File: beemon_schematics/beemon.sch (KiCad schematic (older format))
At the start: 16 parts, among them SW1 SW_SPST, U1 TP4056mini, U2 AMS1117, U3 HD44780_I2C, U4 NodeMCU_1.0_(ESP-12E), U5 HX711

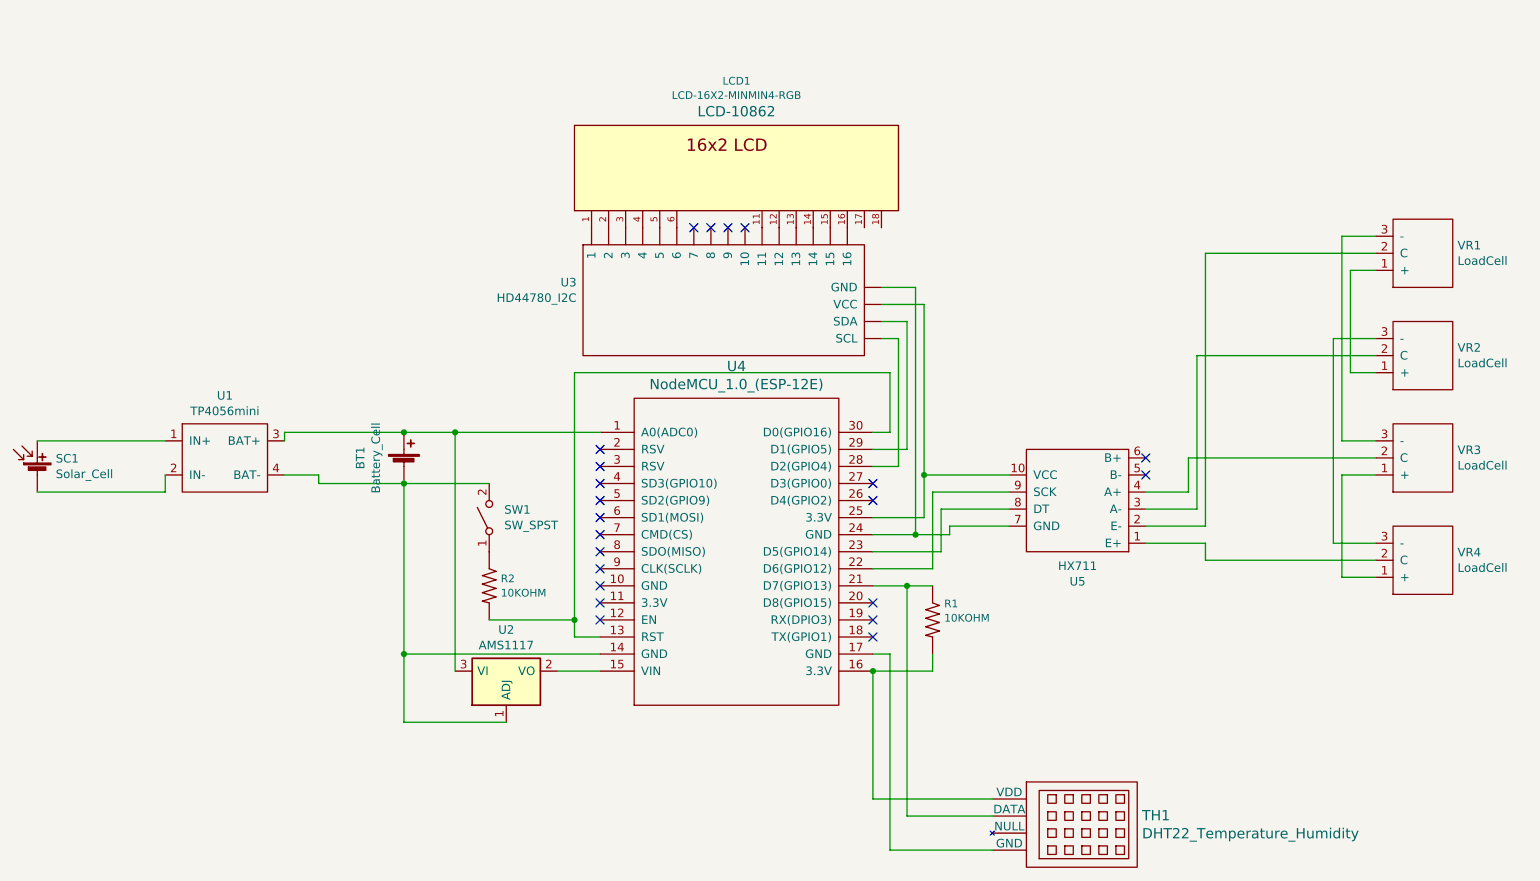
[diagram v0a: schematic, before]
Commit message: Code fixed and tested on 1st prototype. Schematics modified.
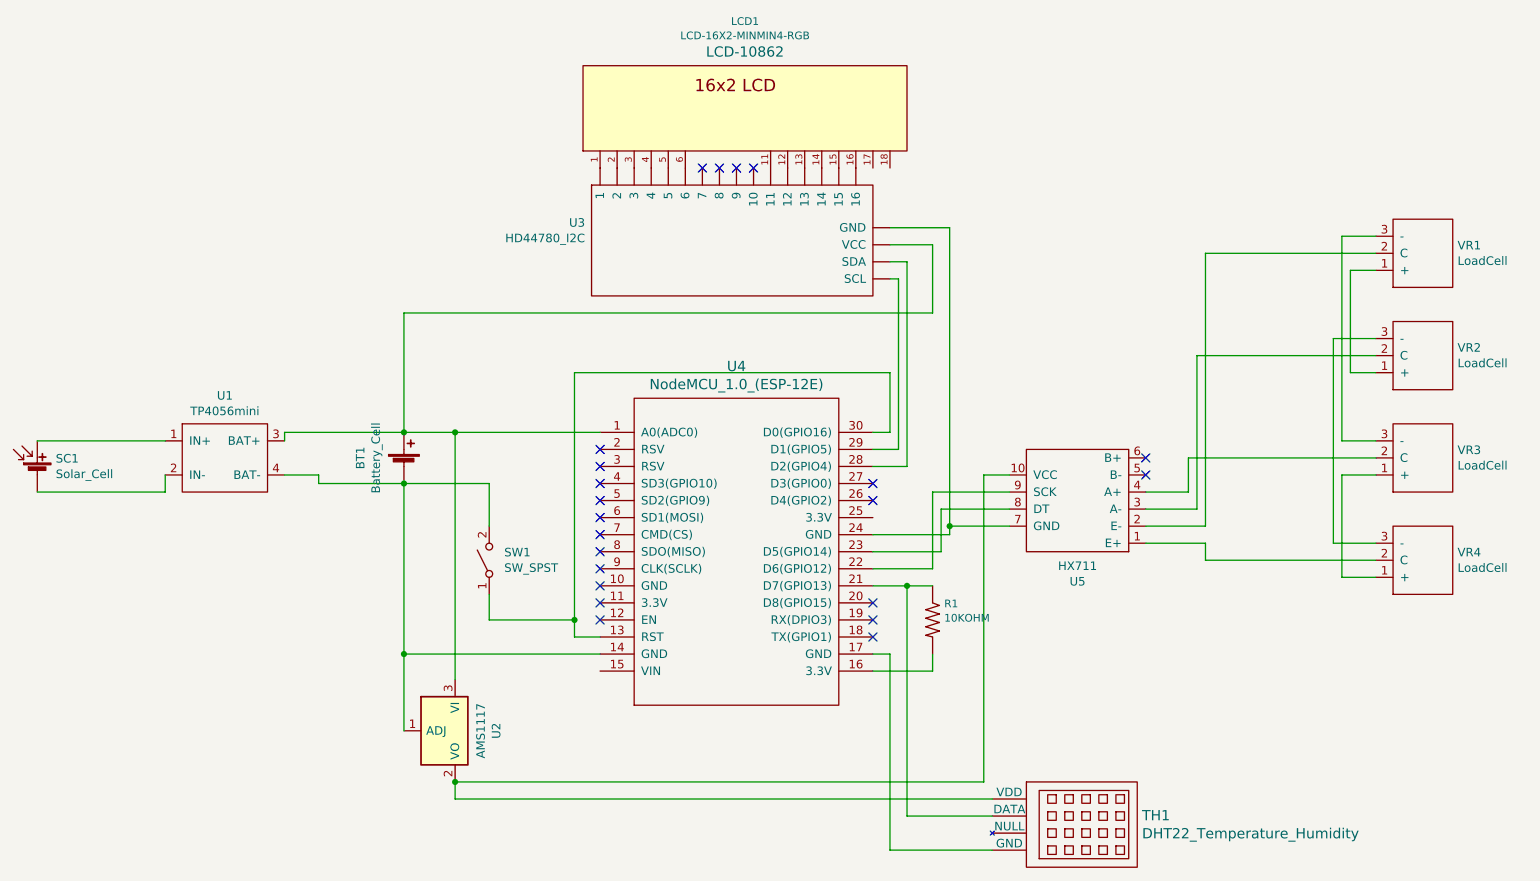
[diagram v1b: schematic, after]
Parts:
- removed R2: 10KOHM, AXIAL-0.3, symbol SparkFun-Resistors:10KOHM-HORIZ-1_4W-1%
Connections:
- net at BT1.1 (+), U1.3 (BAT+), U2.3 (VI)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: now also U3.~ (VCC)
- net at U4.13 (RST), U4.30 (D0(GPIO16)): now also SW1.1 (A)
- net at U4.15 (VIN): no longer U2.2 (VO)
- net at R1.P$2 (2), U4.16 (3.3V): no longer TH1.1 (VDD)
- new net: TH1.1 (VDD), U2.2 (VO), U5.10 (VCC)
- now unconnected: U3.~ (VCC), U4.25 (3.3V)
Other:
- moved on the sheet: LCD1, SW1, U2, U3
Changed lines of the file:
@@
 L Regulator_Linear:AMS1117 U2
 U 1 1 60756942
-P 4450 4950
-F 0 "U2" H 4450 5192 50  0000 C CNN
-F 1 "AMS1117" H 4450 5101 50  0000 C CNN
-F 2 "Package_TO_SOT_SMD:SOT-223-3_TabPin2" H 4450 5150 50  0001 C CNN
-F 3 "http://www.advanced-monolithic.com/pdf/ds1117.pdf" H 4550 4700 50  0001 C CNN
-	1    4450 4950
-	1    0    0    -1
+P 4150 5300
+F 0 "U2" H 4150 5542 50  0000 C CNN
+F 1 "AMS1117" H 4150 5451 50  0000 C CNN
+F 2 "Package_TO_SOT_SMD:SOT-223-3_TabPin2" H 4150 5500 50  0001 C CNN
+F 3 "http://www.advanced-monolithic.com/pdf/ds1117.pdf" H 4250 5050 50  0001 C CNN
+	1    4150 5300
+	0    1    1    0
 $EndComp
 $Comp
@@
 $EndComp
 Wire Wire Line
-	5000 3550 4150 3550
-Wire Wire Line
 	3850 3550 3150 3550
 Wire Wire Line
@@
 Connection ~ 3850 3850
 Wire Wire Line
-	3850 3550 4150 3550
-Connection ~ 4150 3550
-Wire Wire Line
-	4150 3550 4150 4950
-Wire Wire Line
-	4750 4950 5000 4950
-Wire Wire Line
-	4450 5250 3850 5250
-Wire Wire Line
-	3850 5250 3850 4850
-Connection ~ 3850 4850
-Wire Wire Line
 	1700 3600 2450 3600
 Wire Wire Line
 	1700 3900 2450 3900
-Wire Wire Line
-	6600 4950 6600 5700
-Wire Wire Line
-	6600 5700 7300 5700
 Wire Wire Line
 	6600 4850 6700 4850
@@
 Wire Wire Line
 	6950 4950 6600 4950
-Connection ~ 6600 4950
 Wire Wire Line
 	9550 2600 9400 2600
@@
 	7050 4100 7050 4150
 Wire Wire Line
-	7050 4150 6850 4150
-Wire Wire Line
 	7400 4000 7000 4000
 Wire Wire Line
@@
 	7000 4250 6600 4250
 Wire Wire Line
-	7400 3900 6950 3900
-Wire Wire Line
 	6950 3900 6950 4350
 Wire Wire Line
 	6950 4350 6600 4350
-Wire Wire Line
-	6600 4050 6900 4050
-Wire Wire Line
-	6900 3800 7400 3800
-Wire Wire Line
-	6900 2800 6900 3800
-Connection ~ 6900 3800
-Wire Wire Line
-	6900 3800 6900 4050
-Wire Wire Line
-	6850 2700 6850 4150
-Connection ~ 6850 4150
-Wire Wire Line
-	6850 4150 6600 4150
-Wire Wire Line
-	6800 2900 6800 3650
-Wire Wire Line
-	6800 3650 6600 3650
-Wire Wire Line
-	6750 3000 6750 3750
-Wire Wire Line
-	6750 3750 6600 3750
 NoConn ~ 5000 3650
 NoConn ~ 5000 3750
@@
 L Switch:SW_SPST SW1
 U 1 1 607C3174
-P 4350 4050
-F 0 "SW1" V 4396 3962 50  0000 R CNN
-F 1 "SW_SPST" V 4305 3962 50  0000 R CNN
-F 2 "" H 4350 4050 50  0001 C CNN
-F 3 "~" H 4350 4050 50  0001 C CNN
-	1    4350 4050
-	0    -1   -1   0
-$EndComp
-$Comp
-L SparkFun-Resistors:10KOHM-HORIZ-1_4W-1% R2
-U 1 1 607C4ED1
-P 4350 4450
-F 0 "R2" V 4308 4518 45  0000 L CNN
-F 1 "10KOHM" V 4392 4518 45  0000 L CNN
-F 2 "AXIAL-0.3" H 4350 4600 20  0001 C CNN
-F 3 "" H 4350 4450 60  0001 C CNN
-F 4 "" V 4434 4518 60  0000 L CNN "Field4"
-	1    4350 4450
-	0    1    1    0
+P 4350 4300
+F 0 "SW1" V 4396 4212 50  0000 R CNN
+F 1 "SW_SPST" V 4305 4212 50  0000 R CNN
+F 2 "" H 4350 4300 50  0001 C CNN
+F 3 "~" H 4350 4300 50  0001 C CNN
+	1    4350 4300
+	0    -1   -1   0
 $EndComp
 Wire Wire Line
@@
 Wire Wire Line
 	4350 3850 3850 3850
-Wire Wire Line
-	6650 2800 6900 2800
-Wire Wire Line
-	6650 2900 6800 2900
-Wire Wire Line
-	6650 3000 6750 3000
-Wire Wire Line
-	6650 2700 6850 2700
-NoConn ~ 5750 2350
-NoConn ~ 5650 2350
-NoConn ~ 5550 2350
-NoConn ~ 5850 2350
+NoConn ~ 5800 2000
+NoConn ~ 5700 2000
+NoConn ~ 5600 2000
+NoConn ~ 5900 2000
 $Comp
 L Components:HD44780_I2C U3
 U 1 1 60782267
-P 5750 2800
-F 0 "U3" H 4862 2929 50  0000 R CNN
-F 1 "HD44780_I2C" H 4862 2838 50  0000 R CNN
-F 2 "" H 5450 3200 50  0001 C CNN
-F 3 "" H 5450 3200 50  0001 C CNN
-	1    5750 2800
+P 5800 2450
+F 0 "U3" H 4912 2579 50  0000 R CNN
+F 1 "HD44780_I2C" H 4912 2488 50  0000 R CNN
+F 2 "" H 5500 2850 50  0001 C CNN
+F 3 "" H 5500 2850 50  0001 C CNN
+	1    5800 2450
 	1    0    0    -1
 $EndComp
@@
 L SparkFun-Displays:LCD-16X2-MINMIN4-RGB LCD1
 U 1 1 60779C8D
-P 5750 1950
-F 0 "LCD1" V 6210 1900 45  0000 C CNN
-F 1 "LCD-16X2-MINMIN4-RGB" V 6126 1900 45  0000 C CNN
-F 2 "LCD-16X2_NOSILK-KIT-4BIT" H 5750 3050 20  0001 C CNN
-F 3 "" H 5750 1950 50  0001 C CNN
-F 4 "LCD-10862" V 6031 1900 60  0000 C CNN "Field4"
-	1    5750 1950
-	0    -1   -1   0
-$EndComp
+P 5800 1600
+F 0 "LCD1" V 6260 1550 45  0000 C CNN
+F 1 "LCD-16X2-MINMIN4-RGB" V 6176 1550 45  0000 C CNN
+F 2 "LCD-16X2_NOSILK-KIT-4BIT" H 5800 2700 20  0001 C CNN
+F 3 "" H 5800 1600 50  0001 C CNN
+F 4 "LCD-10862" V 6081 1550 60  0000 C CNN "Field4"
+	1    5800 1600
+	0    -1   -1   0
+$EndComp
+Wire Wire Line
+	6750 3650 6600 3650
+Wire Wire Line
+	6800 3750 6600 3750
+Wire Wire Line
+	6600 4150 7050 4150
+Wire Wire Line
+	7400 3900 6950 3900
+Wire Wire Line
+	7050 4100 7050 2350
+Wire Wire Line
+	7050 2350 6700 2350
+Connection ~ 7050 4100
+Wire Wire Line
+	6800 3750 6800 2550
+Wire Wire Line
+	6800 2550 6700 2550
+Wire Wire Line
+	6750 3650 6750 2650
+Wire Wire Line
+	6750 2650 6700 2650
+Wire Wire Line
+	6700 2450 6950 2450
+Wire Wire Line
+	6950 2450 6950 2850
+Wire Wire Line
+	6950 2850 3850 2850
+Wire Wire Line
+	3850 3550 4150 3550
+Wire Wire Line
+	4150 5000 4150 3550
+Connection ~ 4150 3550
+Wire Wire Line
+	4150 3550 5000 3550
+Wire Wire Line
+	3850 5300 3850 4850
+Connection ~ 3850 4850
+Wire Wire Line
+	3850 2850 3850 3550
+Wire Wire Line
+	4150 5700 4150 5600
+Wire Wire Line
+	4150 5700 7300 5700
+Wire Wire Line
+	7400 3800 7250 3800
+Wire Wire Line
+	7250 3800 7250 5600
+Wire Wire Line
+	7250 5600 4150 5600
+Connection ~ 4150 5600
+Wire Wire Line
+	4350 4650 4350 4500
+Wire Wire Line
+	4350 3850 4350 4100
 $EndSCHEMATC

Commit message: Fix schematics error
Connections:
- net at BT1.1 (+), U1.3 (BAT+), U2.3 (VI)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: now also U4.15 (VIN)
- net at U4.13 (RST), U4.30 (D0(GPIO16)): now also SW1.2 (B); no longer SW1.1 (A)
- net at BT1.2 (-), U1.4 (BAT-), U2.1 (ADJ)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: now also SW1.1 (A); no longer SW1.2 (B)
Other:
- moved on the sheet: SW1
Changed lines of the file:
@@
 	3350 3850 3850 3850
 Wire Wire Line
-	3850 3850 3850 4850
+	3850 3850 3850 4750
 Wire Wire Line
 	3850 4850 5000 4850
@@
 	6700 3200 4850 3200
 Wire Wire Line
-	4850 3200 4850 4650
-Wire Wire Line
 	4850 4750 5000 4750
 $Comp
 L Switch:SW_SPST SW1
 U 1 1 607C3174
-P 4350 4300
-F 0 "SW1" V 4396 4212 50  0000 R CNN
-F 1 "SW_SPST" V 4305 4212 50  0000 R CNN
-F 2 "" H 4350 4300 50  0001 C CNN
-F 3 "~" H 4350 4300 50  0001 C CNN
-	1    4350 4300
-	0    -1   -1   0
-$EndComp
-Wire Wire Line
-	4350 4650 4850 4650
-Connection ~ 4850 4650
-Wire Wire Line
-	4850 4650 4850 4750
-Wire Wire Line
-	4350 3850 3850 3850
+P 4450 4750
+F 0 "SW1" V 4496 4662 50  0000 R CNN
+F 1 "SW_SPST" V 4405 4662 50  0000 R CNN
+F 2 "" H 4450 4750 50  0001 C CNN
+F 3 "~" H 4450 4750 50  0001 C CNN
+	1    4450 4750
+	1    0    0    -1
+$EndComp
 NoConn ~ 5800 2000
 NoConn ~ 5700 2000
@@
 Connection ~ 4150 3550
 Wire Wire Line
-	4150 3550 5000 3550
-Wire Wire Line
 	3850 5300 3850 4850
 Connection ~ 3850 4850
@@
 Connection ~ 4150 5600
 Wire Wire Line
-	4350 4650 4350 4500
-Wire Wire Line
-	4350 3850 4350 4100
+	4850 3200 4850 4750
+Wire Wire Line
+	4150 3550 4750 3550
+Wire Wire Line
+	5000 4950 4750 4950
+Wire Wire Line
+	4750 4950 4750 3550
+Connection ~ 4750 3550
+Wire Wire Line
+	4750 3550 5000 3550
+Wire Wire Line
+	4850 4750 4650 4750
+Connection ~ 4850 4750
+Wire Wire Line
+	4250 4750 3850 4750
+Connection ~ 3850 4750
+Wire Wire Line
+	3850 4750 3850 4850
 $EndSCHEMATC

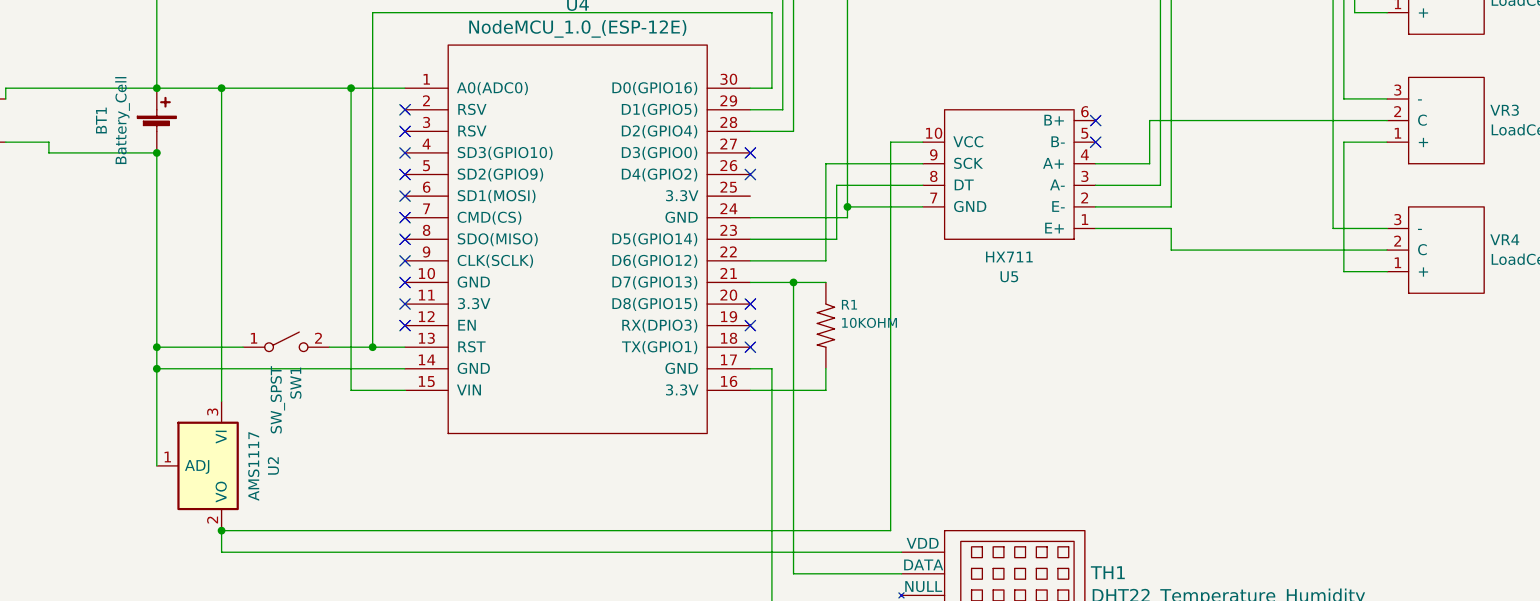
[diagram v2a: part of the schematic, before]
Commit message: Clean weight sensor board, good weight readings
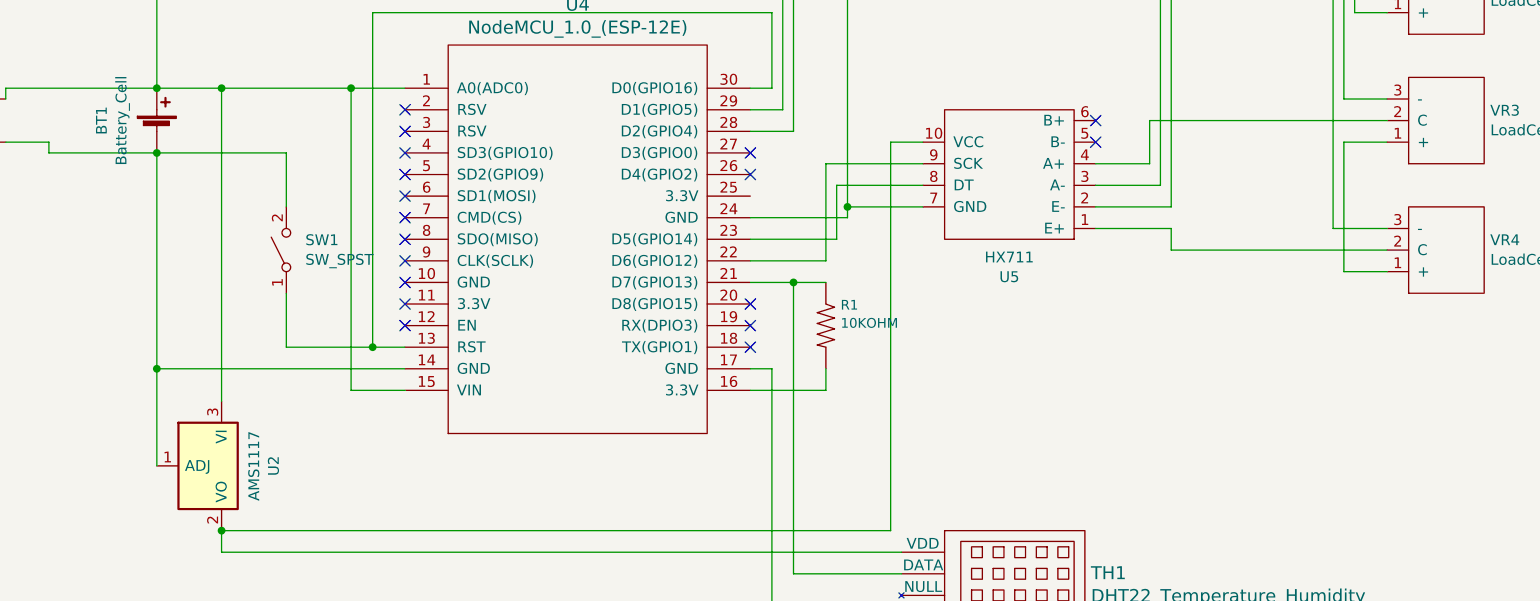
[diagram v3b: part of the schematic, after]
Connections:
- net at U4.13 (RST), U4.30 (D0(GPIO16)): now also SW1.1 (A); no longer SW1.2 (B)
- net at BT1.2 (-), U1.4 (BAT-), U2.1 (ADJ)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: now also SW1.2 (B); no longer SW1.1 (A)
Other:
- moved on the sheet: SW1
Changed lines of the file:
@@
 Title "BeeMon"
 Date "2021-04-13"
-Rev "1.0"
+Rev "1.1"
 Comp ""
 Comment1 ""
@@
 Wire Wire Line
 	3350 3850 3850 3850
-Wire Wire Line
-	3850 3850 3850 4750
 Wire Wire Line
 	3850 4850 5000 4850
@@
 Wire Wire Line
 	8450 3900 8200 3900
-Wire Wire Line
-	9550 4300 8550 4300
 Wire Wire Line
 	8550 4300 8550 4200
@@
 NoConn ~ 6600 4650
 NoConn ~ 6600 4750
-NoConn ~ 8200 3700
-NoConn ~ 8200 3800
 Wire Wire Line
 	6600 3550 6700 3550
@@
 L Switch:SW_SPST SW1
 U 1 1 607C3174
-P 4450 4750
-F 0 "SW1" V 4496 4662 50  0000 R CNN
-F 1 "SW_SPST" V 4405 4662 50  0000 R CNN
-F 2 "" H 4450 4750 50  0001 C CNN
-F 3 "~" H 4450 4750 50  0001 C CNN
-	1    4450 4750
-	1    0    0    -1
+P 4450 4300
+F 0 "SW1" V 4496 4212 50  0000 R CNN
+F 1 "SW_SPST" V 4405 4212 50  0000 R CNN
+F 2 "" H 4450 4300 50  0001 C CNN
+F 3 "~" H 4450 4300 50  0001 C CNN
+	1    4450 4300
+	0    -1   -1   0
 $EndComp
 NoConn ~ 5800 2000
@@
 	4750 3550 5000 3550
 Wire Wire Line
-	4850 4750 4650 4750
+	3850 3850 3850 4850
+Wire Wire Line
+	4850 4750 4450 4750
+Wire Wire Line
+	4450 4750 4450 4500
 Connection ~ 4850 4750
 Wire Wire Line
-	4250 4750 3850 4750
-Connection ~ 3850 4750
-Wire Wire Line
-	3850 4750 3850 4850
+	4450 4100 4450 3850
+Wire Wire Line
+	4450 3850 3850 3850
+Wire Wire Line
+	8550 4300 9550 4300
+NoConn ~ 8200 3700
+NoConn ~ 8200 3800
 $EndSCHEMATC
